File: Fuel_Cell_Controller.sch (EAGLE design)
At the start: 22 parts, among them U1 MAX232PTH

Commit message: Started Fans Schematic
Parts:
- added U$3: SN74LVC245AN, FCC_parts:SN74LVC245AN
- added U$4, U$5, U$6: H11L1H11L1, FCC_parts:H11L1H11L1
- added U$7, U$8, U$9: DMP3056L-7DMP3056L-7, FCC_parts:DMP3056L-7DMP3056L-7
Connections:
- net VALVE_1 renamed SUPPLY_VALVE
- net VALVE_2 renamed PURGE_VALVE
- net VALVE_3 renamed OUTPUT_1
- net VALVE_4 renamed OUTPUT_2
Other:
- note added: "FANS"
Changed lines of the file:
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@@
 <layers>
 <layer number="1" name="Top" color="4" fill="1" visible="no" active="no"/>
+<layer number="2" name="Route2" color="1" fill="3" visible="no" active="no"/>
+<layer number="3" name="Route3" color="4" fill="3" visible="no" active="no"/>
+<layer number="4" name="Route4" color="1" fill="4" visible="no" active="no"/>
+<layer number="5" name="Route5" color="4" fill="4" visible="no" active="no"/>
+<layer number="6" name="Route6" color="1" fill="8" visible="no" active="no"/>
+<layer number="7" name="Route7" color="4" fill="8" visible="no" active="no"/>
+<layer number="8" name="Route8" color="1" fill="2" visible="no" active="no"/>
+<layer number="9" name="Route9" color="4" fill="2" visible="no" active="no"/>
+<layer number="10" name="Route10" color="1" fill="7" visible="no" active="no"/>
+<layer number="11" name="Route11" color="4" fill="7" visible="no" active="no"/>
+<layer number="12" name="Route12" color="1" fill="5" visible="no" active="no"/>
+<layer number="13" name="Route13" color="4" fill="5" visible="no" active="no"/>
+<layer number="14" name="Route14" color="1" fill="6" visible="no" active="no"/>
+<layer number="15" name="Route15" color="4" fill="6" visible="no" active="no"/>
 <layer number="16" name="Bottom" color="1" fill="1" visible="no" active="no"/>
 <layer number="17" name="Pads" color="2" fill="1" visible="no" active="no"/>
@@
 <part name="GND3" library="E-P-008-R1.2" deviceset="GND" device=""/>
 <part name="X2" library="con-subd" library_urn="urn:adsk.eagle:library:189" deviceset="F09" device="HP" package3d_urn="urn:adsk.eagle:package:10232/1"/>
+<part name="U$3" library="FCC_parts" deviceset="SN74LVC245AN" device=""/>
+<part name="U$4" library="FCC_parts" deviceset="H11L1" device="H11L1"/>
+<part name="U$5" library="FCC_parts" deviceset="H11L1" device="H11L1"/>
+<part name="U$6" library="FCC_parts" deviceset="H11L1" device="H11L1"/>
+<part name="U$7" library="FCC_parts" deviceset="DMP3056L-7" device="DMP3056L-7"/>
+<part name="U$8" library="FCC_parts" deviceset="DMP3056L-7" device="DMP3056L-7"/>
+<part name="U$9" library="FCC_parts" deviceset="DMP3056L-7" device="DMP3056L-7"/>
 </parts>
 <sheets>
@@
 <text x="99.06" y="215.9" size="1.778" layer="94">POWER CONNECTORS</text>
 <text x="20.32" y="-187.96" size="1.778" layer="94">Motor Controller</text>
+<wire x1="-15.24" y1="213.36" x2="-15.24" y2="-243.84" width="0.1524" layer="94"/>
+<wire x1="-15.24" y1="-243.84" x2="86.36" y2="-243.84" width="0.1524" layer="94"/>
+<wire x1="86.36" y1="-243.84" x2="86.36" y2="213.36" width="0.1524" layer="94"/>
+<wire x1="86.36" y1="213.36" x2="-15.24" y2="213.36" width="0.1524" layer="94"/>
+<wire x1="99.06" y1="213.36" x2="223.52" y2="213.36" width="0.1524" layer="94"/>
+<wire x1="223.52" y1="213.36" x2="223.52" y2="134.62" width="0.1524" layer="94"/>
+<wire x1="223.52" y1="134.62" x2="99.06" y2="134.62" width="0.1524" layer="94"/>
+<wire x1="99.06" y1="134.62" x2="99.06" y2="213.36" width="0.1524" layer="94"/>
 </plain>
 <instances>
@@
 </segment>
 </net>
-<net name="VALVE_1" class="0">
+<net name="SUPPLY_VALVE" class="0">
 <segment>
 <pinref part="ETH9" gate="G$1" pin="1"/>
@@
 </segment>
 </net>
-<net name="VALVE_2" class="0">
+<net name="PURGE_VALVE" class="0">
 <segment>
 <pinref part="ETH9" gate="G$1" pin="3"/>
@@
 </segment>
 </net>
-<net name="VALVE_3" class="0">
+<net name="OUTPUT_1" class="0">
 <segment>
 <pinref part="ETH9" gate="G$1" pin="5"/>
@@
 </segment>
 </net>
-<net name="VALVE_4" class="0">
+<net name="OUTPUT_2" class="0">
 <segment>
 <pinref part="ETH9" gate="G$1" pin="7"/>
@@
 </segment>
 </net>
-<net name="N$1" class="0">
-<segment>
-<wire x1="-17.78" y1="213.36" x2="88.9" y2="213.36" width="0.1524" layer="91"/>
-<wire x1="88.9" y1="213.36" x2="88.9" y2="-246.38" width="0.1524" layer="91"/>
-<wire x1="88.9" y1="-246.38" x2="-17.78" y2="-246.38" width="0.1524" layer="91"/>
-<wire x1="-17.78" y1="-246.38" x2="-17.78" y2="213.36" width="0.1524" layer="91"/>
-</segment>
-</net>
-<net name="N$2" class="0">
-<segment>
-<wire x1="96.52" y1="213.36" x2="231.14" y2="213.36" width="0.1524" layer="91"/>
-<wire x1="231.14" y1="213.36" x2="231.14" y2="129.54" width="0.1524" layer="91"/>
-<wire x1="231.14" y1="129.54" x2="96.52" y2="129.54" width="0.1524" layer="91"/>
-<wire x1="96.52" y1="129.54" x2="96.52" y2="213.36" width="0.1524" layer="91"/>
-</segment>
-</net>
 </nets>
 </sheet>
+<sheet>
+<plain>
+<text x="-7.62" y="83.82" size="1.778" layer="94">FANS</text>
+</plain>
+<instances>
+<instance part="U$3" gate="G$1" x="20.32" y="48.26"/>
+<instance part="U$4" gate="G$1" x="81.28" y="66.04"/>
+<instance part="U$5" gate="G$1" x="81.28" y="43.18"/>
+<instance part="U$6" gate="G$1" x="81.28" y="20.32"/>
+<instance part="U$7" gate="G$1" x="134.62" y="58.42"/>
+<instance part="U$8" gate="G$1" x="134.62" y="30.48"/>
+<instance part="U$9" gate="G$1" x="134.62" y="5.08"/>
+</instances>
+<busses>
+</busses>
+<nets>
+</nets>
+</sheet>

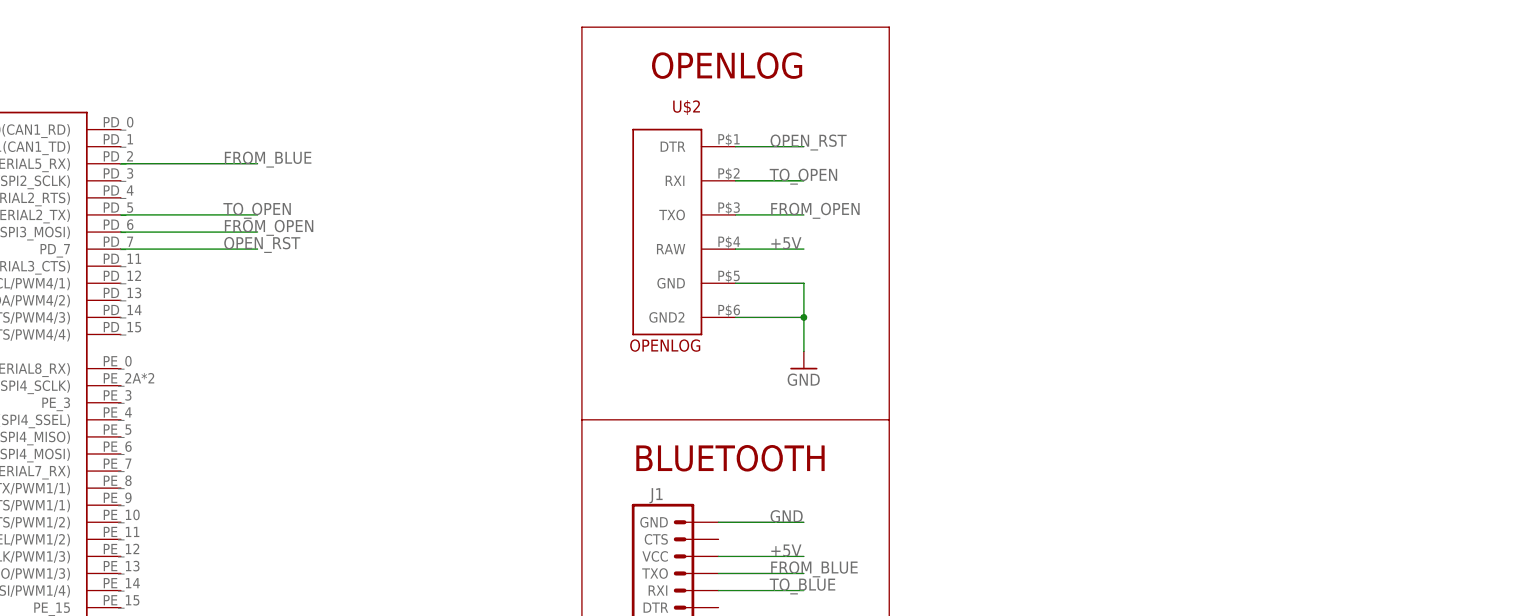
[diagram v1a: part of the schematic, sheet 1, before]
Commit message: Implemented FTDI Chip on the schematic
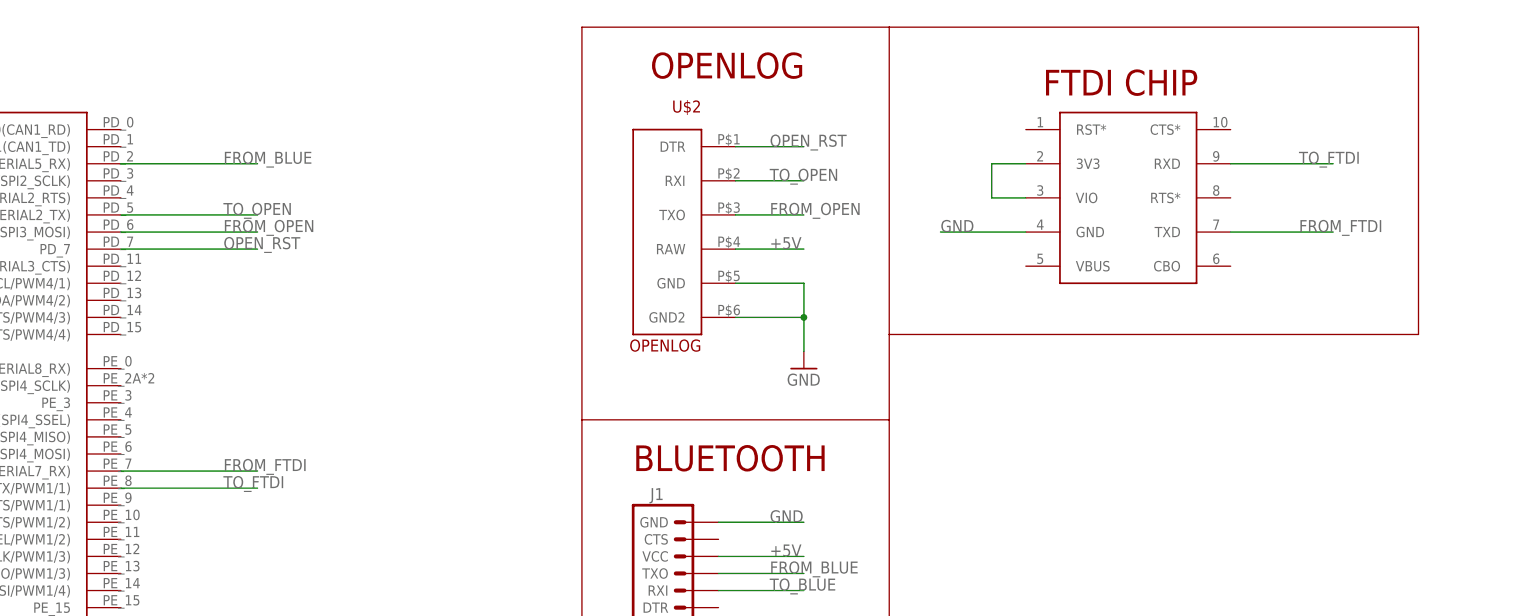
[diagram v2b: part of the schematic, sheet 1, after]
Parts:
- added U$10: UMFT234XFUMFT234XF, FCC_parts:UMFT234XFUMFT234XF
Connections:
- new net FROM_FTDI: U$1.PE_7(SERIAL7_RX), U$10.TXD
- new net N$1: U$10.3V3, U$10.VIO
- new net TO_FTDI: U$1.PE_8(SERIAL7_TX/PWM1/1), U$10.RXD
- net GND: now also U$10.GND
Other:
- note added: "FTDI CHIP"
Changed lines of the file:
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@@
 <part name="U$8" library="FCC_parts" deviceset="DMP3056L-7" device="DMP3056L-7"/>
 <part name="U$9" library="FCC_parts" deviceset="DMP3056L-7" device="DMP3056L-7"/>
+<part name="U$10" library="FCC_parts" deviceset="UMFT234XF" device="UMFT234XF"/>
 </parts>
 <sheets>
@@
 <text x="149.86" y="71.12" size="3.81" layer="94">OPENLOG</text>
 <wire x1="139.7" y1="78.74" x2="185.42" y2="78.74" width="0.1524" layer="94"/>
-<wire x1="185.42" y1="78.74" x2="185.42" y2="20.32" width="0.1524" layer="94"/>
+<wire x1="185.42" y1="78.74" x2="185.42" y2="33.02" width="0.1524" layer="94"/>
+<wire x1="185.42" y1="33.02" x2="185.42" y2="20.32" width="0.1524" layer="94"/>
 <wire x1="185.42" y1="20.32" x2="139.7" y2="20.32" width="0.1524" layer="94"/>
 <wire x1="139.7" y1="20.32" x2="139.7" y2="78.74" width="0.1524" layer="94"/>
@@
 <wire x1="307.34" y1="-27.94" x2="307.34" y2="-68.58" width="0.1524" layer="94"/>
 <wire x1="307.34" y1="-68.58" x2="210.82" y2="-68.58" width="0.1524" layer="94"/>
+<text x="208.28" y="68.58" size="3.81" layer="94">FTDI CHIP</text>
+<wire x1="185.42" y1="78.74" x2="264.16" y2="78.74" width="0.1524" layer="94"/>
+<wire x1="264.16" y1="78.74" x2="264.16" y2="33.02" width="0.1524" layer="94"/>
+<wire x1="264.16" y1="33.02" x2="185.42" y2="33.02" width="0.1524" layer="94"/>
 </plain>
 <instances>
@@
 <instance part="GND3" gate="1" x="198.12" y="-58.42"/>
 <instance part="X2" gate="G$1" x="259.08" y="-53.34"/>
+<instance part="U$10" gate="G$1" x="220.98" y="53.34"/>
 </instances>
 <busses>
@@
 <wire x1="251.46" y1="-58.42" x2="231.14" y2="-58.42" width="0.1524" layer="91"/>
 <label x="231.14" y="-58.42" size="1.778" layer="95"/>
+</segment>
+<segment>
+<pinref part="U$10" gate="G$1" pin="GND"/>
+<wire x1="205.74" y1="48.26" x2="193.04" y2="48.26" width="0.1524" layer="91"/>
+<label x="193.04" y="48.26" size="1.778" layer="95"/>
 </segment>
 </net>
@@
 </segment>
 </net>
+<net name="N$1" class="0">
+<segment>
+<pinref part="U$10" gate="G$1" pin="3V3"/>
+<wire x1="205.74" y1="58.42" x2="200.66" y2="58.42" width="0.1524" layer="91"/>
+<wire x1="200.66" y1="58.42" x2="200.66" y2="53.34" width="0.1524" layer="91"/>
+<pinref part="U$10" gate="G$1" pin="VIO"/>
+<wire x1="200.66" y1="53.34" x2="205.74" y2="53.34" width="0.1524" layer="91"/>
+</segment>
+</net>
+<net name="TO_FTDI" class="0">
+<segment>
+<pinref part="U$10" gate="G$1" pin="RXD"/>
+<wire x1="236.22" y1="58.42" x2="251.46" y2="58.42" width="0.1524" layer="91"/>
+<label x="246.38" y="58.42" size="1.778" layer="95"/>
+</segment>
+<segment>
+<pinref part="U$1" gate="G$1" pin="PE_8(SERIAL7_TX/PWM1/1)"/>
+<wire x1="71.12" y1="10.16" x2="91.44" y2="10.16" width="0.1524" layer="91"/>
+<label x="86.36" y="10.16" size="1.778" layer="95"/>
+</segment>
+</net>
+<net name="FROM_FTDI" class="0">
+<segment>
+<pinref part="U$10" gate="G$1" pin="TXD"/>
+<wire x1="236.22" y1="48.26" x2="251.46" y2="48.26" width="0.1524" layer="91"/>
+<label x="246.38" y="48.26" size="1.778" layer="95"/>
+</segment>
+<segment>
+<pinref part="U$1" gate="G$1" pin="PE_7(SERIAL7_RX)"/>
+<wire x1="71.12" y1="12.7" x2="91.44" y2="12.7" width="0.1524" layer="91"/>
+<label x="86.36" y="12.7" size="1.778" layer="95"/>
+</segment>
+</net>

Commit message: added some connections
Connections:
- removed net ESTOP1: ETH6.3
- removed net ESTOP2: ETH6.4
- new net ESTOP_1: ETH6.3, U$1.PB_12(CAN2_RD/SPI2_SSEL)
- new net ESTOP_2: ETH6.4, U$1.PB_13(SERIAL3_CTS/CAN2_TD/SPI2_SCLK/PWM1/1)
- new net N$10: U$6.GND
- new net N$2: U$4.GND
- new net N$9: U$5.GND
- net CAP_CURR: now also U$1.PA_7(D11/ANALOGIN/SPI1_MOSI)
- net CAP_RELAY: now also U$1.PB_2(SPI3_MOSI)
- net CAP_VOLT: now also U$1.PA_4(ANALOGOUT/ANALOGIN/SPI1_SSEL)
- net CHARGE_RELAY: now also U$1.PB_4(SPI2_SSEL/SPI1_MISO/PWM3/1)
- net FCC_RELAY: now also U$1.PB_0(LED1)
- net FC_CURR: now also U$1.PA_5(D13/ANALOGOUT/ANALOGIN/SPI1_SCLK/PWM2/1)
- net FC_VOLT: now also U$1.PA_0(SERIAL4_TX/ANALOGIN/SERIAL2_CTS/PWM2/1)
- net H2_OK: now also U$1.PB_6(SERIAL1_TX/CAN2_TD/I2C1_SCL/PWM4/1)
- net MOTOR_CURR: now also U$1.PA_6(D12/ANALOGIN/SPI1_MISO/PWM3/1)
- net MOTOR_RELAY: now also U$1.PB_3(SPI1_SCLK/PWM2/2)
- net MOTOR_VOLT: now also U$1.PA_3(A0/ANALOGIN/SERIAL2_RX/PWM2/4)
- net OUTPUT_1: now also U$1.PD_0(CAN1_RD)
- net OUTPUT_2: now also U$1.PD_1(CAN1_TD)
- net PRESSURE_1: now also U$1.PB_1(ANALOGIN/PWM1/3)
- net PRESSURE_2: now also U$1.PC_0(A1/ANALOGIN)
- net PRESSURE_3: now also U$1.PC_2(ANALOGIN/SPI2_MISO)
- net PRESSURE_4: now also U$1.PC_3(A2/ANALOGIN/SPI2_MOSI)
- net PURGE_VALVE: now also U$1.PC_11(SERIAL4_RX/SPI3_MISO)
- net STOP: now also U$1.PB_5(CAN2_RD/SPI1_MOSI/PWM3/2)
- net SUPPLY_VALVE: now also U$1.PC_10(SERIAL3_TX/SPI3_SCLK)
- net TACH_1: now also U$1.PB_15(SPI2_MOSI/PWM12/2)
- net TACH_2: now also U$1.PC_8(SERIAL5_RTS/PWM8/3)
- net TACH_3: now also U$1.PC_9(I2C3_SDA/SERIAL5_CTS/PWM8/4)

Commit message: added a few connections
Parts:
- removed ETH10: ETHERNET, ETHERNET:ETHERNET
- removed U$5, U$6: H11L1H11L1, FCC_parts:H11L1H11L1
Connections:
- removed net N$10: U$6.GND
- new net FANS_SWITCH_ALL: U$1.PE_3, U$4.ANODE
- net FCTEMP_1: now also U$1.PF_3(A3/ANALOGIN)
- net FCTEMP_2: now also U$1.PF_4(ANALOGIN)
- net GND: now also U$4.CATHODE
- net N$9: now also U$4.VCC; no longer U$5.GND
- net PWM_1: now also U$1.PE_11(D5/SPI4_SSEL/PWM1/2)
- net PWM_2: now also U$1.PE_12(SPI4_SCLK/PWM1/3)
- net PWM_3: now also U$1.PE_14(SPI4_MOSI/PWM1/4)
- net TEMP_1: now also U$1.PF_5(A4/ANALOGIN)
- net TEMP_2: now also U$1.PF_7(PWM11/1/ANALOGIN/SERIAL7_TX/SPI5_SCLK)
- net TEMP_3: now also U$1.PF_8(PWM13/1/ANALOGIN/SERIAL7_RTS/SPI5_MISO)
- net TEMP_4: now also U$1.PF_9(PWM14/1/ANALOGIN/SERIAL7_CTS/SPI5_MOSI)
- net TEMP_5: now also U$1.PF_10(A5/ANALOGIN)
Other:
- note removed: "Motor Controller"
- moved on the sheet: U$3, X2
